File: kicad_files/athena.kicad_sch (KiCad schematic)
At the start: 619 parts, among them J1 TYPE-C-31-M-12, J2 A1001WR-S-04P, Q1 2N7002, Q2 2N7002, Q3 AO3401A, Q4 2N7002, Q5 2N7002, Q6 2N7002, Q7 2N7002, Q8 2N7002, SW1 K2-1187SQ-A4SW-06, SW10 MX Switch, SW100 MX Switch, SW101 MX Switch, SW102 MX Switch, SW103 MX Switch, SW104 MX Switch, SW105 MX Switch, SW106 MX Switch, SW107 MX Switch, SW108 MX Switch, SW109 MX Switch, SW11 MX Switch, SW110 MX Switch, SW111 MX Switch, SW112 MX Switch, SW113 MX Switch, SW114 MX Switch, SW115 MX Switch, SW116 MX Switch, SW117 MX Switch, SW118 MX Switch, SW119 MX Switch, SW12 MX Switch, SW120 MX Switch, SW13 MX Switch, SW14 MX Switch, SW15 MX Switch, SW16 MX Switch, SW17 MX Switch, SW18 MX Switch, SW19 MX Switch, SW2 MX Switch, SW20 MX Switch, SW21 MX Switch, SW22 MX Switch, SW23 MX Switch, SW24 MX Switch, SW25 MX Switch, SW26 MX Switch, SW27 MX Switch, SW28 MX Switch, SW29 MX Switch, SW3 MX Switch, SW30 MX Switch, SW31 MX Switch, SW32 MX Switch, SW33 MX Switch, SW34 MX Switch, SW35 MX Switch, SW36 MX Switch, SW37 MX Switch, SW38 MX Switch, SW39 MX Switch, SW4 MX Switch, SW40 MX Switch, SW41 MX Switch, SW42 MX Switch, SW43 MX Switch, SW44 MX Switch, SW45 MX Switch, SW46 MX Switch, SW47 MX Switch, SW48 MX Switch, SW49 MX Switch, SW5 MX Switch, SW50 MX Switch, SW51 MX Switch, SW52 MX Switch, SW53 MX Switch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

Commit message: DRC ran, no issues found,, schematic cleaned up
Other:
- note removed: "RGB STRIP"
- moved on the sheet: C18, C19, C20, C21, C22, C23, C24, C25, C26, C27, C28, C29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

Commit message: Adjustments for LDO and RGB level translator due to no stock
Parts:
- removed C12: 10n, Capacitor_SMD:C_0402_1005Metric, symbol Device:C_Small
- removed U4: SGM2007-3.3XN5/TR, acheron_Components:SOT-23-5, symbol acheron_Symbols:SGM2036
- added U4: AP7333, Package_TO_SOT_SMD:SOT-23, symbol acheron_Symbols:UR133AG-33_SOT-89-3
- U5: value TXS0101DRLR -> TXS0101DCKR; footprint acheron_Components:SOT-563 -> acheron_Components:SOT-363_SC-70-6; Manufacturer Part Number TXS0101DRLR -> TXS0101DCKR; Package SOT-563 -> SC-70-6; Vendor Part Number LCSC C131928 -> LCSC C132031
- X1: renamed from X4; now left out of the parts list
- X4: renamed from X3; now left out of the parts list
- renumbered C11 to C10, C13 to C11, C14 to C12, C15 to C13, C16 to C14, C17 to C15, C21 to C16, C22 to C17, C23 to C18, C24 to C19, C25 to C20, C26 to C21, C27 to C22, C28 to C23, C29 to C24, C30 to C25, C31 to C26, C32 to C27, C33 to C28, C34 to C29, C35 to C30, C36 to C31, C37 to C32, C18 to C33, C19 to C34, C20 to C35, C9 to C36, C38 to C37, C39 to C38, C40 to C39, C41 to C40, C42 to C41, C43 to C42, C44 to C43, C45 to C44, C46 to C45, C47 to C46, C48 to C47, C49 to C48, C50 to C49, C51 to C50, C10 to C9, D11 to D10, D113 to D100, D114 to D101, D115 to D102, D116 to D103, D118 to D105, D120 to D106, D121 to D107, D122 to D108, D123 to D109, D12 to D11, D124 to D110, D68 to D111, D125 to D112, D119 to D113, D132 to D114, D117 to D115, D133 to D116, D128 to D117, D127 to D118, D126 to D119, D13 to D12, D53 to D120, D52 to D121, D51 to D122, D70 to D123, D69 to D124, D85 to D125, D87 to D126, D86 to D127, D102 to D128, D131 to D129, D14 to D13, D129 to D131, D71 to D132, D15 to D14, D16 to D15, D17 to D16, D18 to D17, D19 to D18, D20 to D19, D21 to D20, D22 to D21, D23 to D22, D24 to D23, D25 to D24, D26 to D25, D27 to D26, D28 to D27, D29 to D28, D30 to D29, D4 to D3, D31 to D30, D32 to D31, D33 to D32, D34 to D33, D35 to D34, D36 to D35, D37 to D36, D38 to D37, D39 to D38, D40 to D39, D5 to D4, D41 to D40, D42 to D41, D43 to D42, D44 to D43, D45 to D44, D46 to D45, D47 to D46, D48 to D47, D49 to D48, D50 to D49, D6 to D5, D54 to D50, D55 to D51, D56 to D52, D57 to D53, D58 to D54, D59 to D55, D60 to D56, D61 to D57, D62 to D58, D63 to D59, D7 to D6, D64 to D60, D65 to D61, D66 to D62, D67 to D63, D72 to D64, D73 to D65, D74 to D66, D75 to D67, D76 to D68, D77 to D69, D8 to D7, D78 to D70, D79 to D71, D80 to D72, D81 to D73, D82 to D74, D83 to D75, D84 to D76, D88 to D77, D89 to D78, D90 to D79, D9 to D8, D91 to D80, D92 to D81, D93 to D82, D94 to D83, D95 to D84, D96 to D85, D97 to D86, D98 to D87, D99 to D88, D100 to D89, D10 to D9, D101 to D90, D103 to D91, D105 to D92, D106 to D93, D107 to D94, D108 to D95, D109 to D96, D110 to D97, D111 to D98, D112 to D99, FB3 to FB1, FB1 to FB2, GR11 to GR10, GR9 to GR11, GR10 to GR8, GR8 to GR9, LED28 to LED1, LED5 to LED10, LED95 to LED100, LED96 to LED101, LED97 to LED102, LED98 to LED103, LED99 to LED104, LED100 to LED105, LED101 to LED106, LED102 to LED107, LED103 to LED108, LED104 to LED109, LED6 to LED11, LED105 to LED110, LED106 to LED111, LED107 to LED112, LED108 to LED113, LED109 to LED114, LED110 to LED115, LED111 to LED116, LED114 to LED117, LED112 to LED118, LED113 to LED119, LED7 to LED12, LED8 to LED13, LED9 to LED14, LED10 to LED15, LED11 to LED16, LED12 to LED17, LED13 to LED18, LED14 to LED19, LED68 to LED2, LED16 to LED20, LED17 to LED21, LED18 to LED22, LED19 to LED23, LED20 to LED24, LED21 to LED25, LED22 to LED26, LED23 to LED27, LED24 to LED28, LED25 to LED29, LED69 to LED3, LED36 to LED30, LED27 to LED31, LED29 to LED32, LED30 to LED33, LED31 to LED34, LED32 to LED35, LED33 to LED36, LED34 to LED37, LED35 to LED38, LED37 to LED39, LED26 to LED4, LED38 to LED40, LED39 to LED41, LED40 to LED42, LED41 to LED43, LED42 to LED44, LED43 to LED45, LED44 to LED46, LED56 to LED47, LED45 to LED48, LED46 to LED49, LED3 to LED5, LED47 to LED50, LED48 to LED51, LED49 to LED52, LED50 to LED53, LED51 to LED54, LED52 to LED55, LED53 to LED56, LED54 to LED57, LED55 to LED58, LED57 to LED59, LED15 to LED6, LED58 to LED60, LED59 to LED61, LED60 to LED62, LED61 to LED63, LED62 to LED64, LED74 to LED65, LED67 to LED66, LED117 to LED67, LED63 to LED68, LED64 to LED69, LED1 to LED7, LED65 to LED70, LED66 to LED71, LED70 to LED72, LED71 to LED73, LED72 to LED74, LED73 to LED75, LED75 to LED76, LED76 to LED77, LED77 to LED78, LED118 to LED79, LED2 to LED8, LED119 to LED80, LED78 to LED81, LED79 to LED82, LED92 to LED83, LED93 to LED84, LED80 to LED85, LED81 to LED86, LED82 to LED87, LED83 to LED88, LED84 to LED89, LED4 to LED9, LED85 to LED90, LED86 to LED91, LED87 to LED92, LED88 to LED93, LED89 to LED94, LED90 to LED95, LED91 to LED96, LED115 to LED97, LED116 to LED98, LED94 to LED99, Q5 to Q3, Q6 to Q4, Q7 to Q5, Q8 to Q6, Q3 to Q7, Q4 to Q8, R11 to R10, R58 to R100, R59 to R101, R60 to R102, R61 to R103, R62 to R104, R64 to R105, R65 to R106, R66 to R107, R67 to R108, R68 to R109, R12 to R11, R69 to R110, R70 to R111, R71 to R112, R72 to R113, R63 to R114, R73 to R115, R75 to R116, R76 to R117, R77 to R118, R83 to R119, R10 to R12, R78 to R120, R80 to R121, R84 to R122, R85 to R123, R86 to R124, R81 to R125, R82 to R126, R145 to R127, R146 to R128, R87 to R129, R144 to R130, R79 to R131, R91 to R132, R93 to R133, R94 to R134, R89 to R135, R90 to R136, R95 to R137, R96 to R138, R97 to R139, R98 to R140, R99 to R141, R100 to R142, R101 to R143, R102 to R144, R103 to R145, R104 to R146, R105 to R147, R138 to R148, R141 to R149, R106 to R150, R107 to R151, R108 to R152, R109 to R153, R110 to R154, R111 to R155, R112 to R156, R113 to R157, R114 to R158, R115 to R159, R134 to R16, R116 to R160, R117 to R161, R135 to R17, R147 to R18, R148 to R19, R149 to R20, R150 to R21, R151 to R22, R152 to R23, R153 to R24, R154 to R25, R155 to R26, R156 to R27, R157 to R28, R158 to R29, R159 to R30, R160 to R31, R161 to R32, R16 to R33, R118 to R34, R119 to R35, R120 to R36, R121 to R37, R122 to R38, R123 to R39, R124 to R40, R125 to R41, R126 to R42, R127 to R43, R128 to R44, R129 to R45, R130 to R46, R131 to R47, R132 to R48, R133 to R49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
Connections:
- net 3V3: now also R11.2, U4.2 (VO); no longer R11.1
- net 5V: now also U4.1 (VI)
- net GND: now also R11.1, U4.3 (GND); no longer R11.2
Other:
- moved on the sheet: D100, D101, D102, D103, D104, D105, D106, D107, D108, D109, D110, D111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

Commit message: New DRC ran, no errors issued. Ready for release
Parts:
- R58, R59, R60, R61: Package R0402 -> R0805
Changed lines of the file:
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@@
     (title "Athena PCB schematic")
     (date "2023-04-26")
-    (rev "V3.0.2")
+    (rev "V3.0.3")
     (company "Acheron Project")
     (comment 1 "Designed by Gondolindrim")
@@
       (effects (font (size 1.27 1.27)) hide)
     )
-    (property "Package" "R0402" (at 279.4 412.75 0)
-      (effects (font (size 1.27 1.27)) hide)
-    )
     (property "Manufacturer" "Uniroyal" (at 279.4 412.75 0)
       (effects (font (size 1.27 1.27)) hide)
@@
       (effects (font (size 1.27 1.27)) hide)
     )
-    (property "Package" "R0402" (at 406.4 412.75 0)
-      (effects (font (size 1.27 1.27)) hide)
-    )
     (property "Manufacturer" "Uniroyal" (at 406.4 412.75 0)
       (effects (font (size 1.27 1.27)) hide)
@@
       (effects (font (size 1.27 1.27)) hide)
     )
-    (property "Package" "R0402" (at 342.9 412.75 0)
-      (effects (font (size 1.27 1.27)) hide)
-    )
     (property "Manufacturer" "Uniroyal" (at 342.9 412.75 0)
       (effects (font (size 1.27 1.27)) hide)
@@
       (effects (font (size 1.27 1.27)) hide)
     )
-    (property "Package" "R0402" (at 215.9 412.75 0)
-      (effects (font (size 1.27 1.27)) hide)
-    )

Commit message: Adjusted LDO footprint
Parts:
- removed U4: AP7333, Package_TO_SOT_SMD:SOT-23, symbol acheron_Symbols:UR133AG-33_SOT-89-3
- added U6: MCP1700T-3302E/TT, Package_TO_SOT_SMD:SOT-23, symbol Regulator_Linear:MCP1700-3302E_SOT23
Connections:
- net 3V3: now also U6.2 (VO)
- net 5V: now also U6.3 (VI)
- net GND: now also U6.1 (GND)
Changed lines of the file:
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@@
   (junction (at 424.815 565.15) (diameter 0) (color 0 0 0 0)
   )
-  (junction (at 908.05 406.4) (diameter 0) (color 0 0 0 0)
-  )
   (junction (at 793.75 419.1) (diameter 1.016) (color 0 0 0 0)
   )
@@
   (junction (at 1047.75 342.9) (diameter 1.016) (color 0 0 0 0)
   )
-  (junction (at 1035.05 434.34) (diameter 0) (color 0 0 0 0)
-  )
   (junction (at 1035.05 330.2) (diameter 0.9144) (color 0 0 0 0)
   )
@@
   (junction (at 189.865 447.04) (diameter 0.9144) (color 0 0 0 0)
   )
-  (junction (at 933.45 406.4) (diameter 0) (color 0 0 0 0)
-  )
   (junction (at 272.415 596.9) (diameter 0) (color 0 0 0 0)
   )
@@
     (stroke (width 0) (type default))
   )
-  (wire (pts (xy 908.05 406.4) (xy 911.86 406.4))
-    (stroke (width 0) (type solid))
-  )
   (wire (pts (xy 200.66 122.555) (xy 193.04 122.555))
     (stroke (width 0) (type solid))
@@
     (stroke (width 0) (type solid))
   )
-  (wire (pts (xy 908.05 406.4) (xy 908.05 408.94))
-    (stroke (width 0) (type solid))
-  )
   (wire (pts (xy 177.165 614.68) (xy 177.165 615.95))
     (stroke (width 0) (type solid))
@@
     (stroke (width 0) (type solid))
   )
-  (wire (pts (xy 1035.05 406.4) (xy 1035.05 434.34))
+  (wire (pts (xy 1035.05 406.4) (xy 1035.05 444.5))
     (stroke (width 0) (type default))
   )
@@
     (stroke (width 0) (type solid))
   )
-  (wire (pts (xy 1035.05 434.34) (xy 1035.05 444.5))
-    (stroke (width 0) (type default))
-  )
   (wire (pts (xy 1009.65 444.5) (xy 1009.65 482.6))
     (stroke (width 0) (type solid))
@@
     (stroke (width 0) (type solid))
   )
+  (wire (pts (xy 908.05 406.4) (xy 911.86 406.4))
+    (stroke (width 0) (type solid))
+  )
   (wire (pts (xy 139.065 438.15) (xy 139.065 440.69))
     (stroke (width 0) (type solid))
@@
     (stroke (width 0) (type solid))
   )
-  (wire (pts (xy 1034.415 434.34) (xy 1035.05 434.34))
-    (stroke (width 0) (type default))
-  )
   (wire (pts (xy 1060.45 635) (xy 1064.26 635))
     (stroke (width 0) (type solid))
@@
     (stroke (width 0) (type solid))
   )
-  (wire (pts (xy 520.7 114.3) (xy 520.7 115.57))
-    (stroke (width 0) (type solid))
-  )
   (wire (pts (xy 1014.73 255.27) (xy 1013.46 255.27))
     (stroke (width 0) (type solid))
@@
     (stroke (width 0) (type solid))
   )
-  (wire (pts (xy 933.45 406.4) (xy 933.45 408.94))
-    (stroke (width 0) (type solid))
-  )
   (wire (pts (xy 418.465 607.06) (xy 418.465 606.425))
     (stroke (width 0) (type default))
@@
     )
   )
+  (symbol (lib_id "Regulator_Linear:MCP1700-3302E_SOT23") (at 520.7 107.95 0) (unit 1)
+    (in_bom yes) (on_board yes) (dnp no)
+    (property "Reference" "U6" (at 520.7 101.6 0)
+      (effects (font (size 1.27 1.27)))
+    )
+    (property "Value" "MCP1700T-3302E/TT" (at 520.7 103.505 0)
+      (effects (font (size 0.762 0.762)))
+    )
+    (property "Footprint" "Package_TO_SOT_SMD:SOT-23" (at 520.7 102.235 0)
+      (effects (font (size 1.27 1.27)) hide)
+    )
+    (property "Datasheet" "http://ww1.microchip.com/downloads/en/DeviceDoc/20001826D.pdf" (at 520.7 107.95 0)
+      (effects (font (size 1.27 1.27)) hide)
+    )
+    (property "Manufacturer Part Number" "MCP1700T-3302E/TT" (at 520.7 107.95 0)
+      (effects (font (size 1.27 1.27)) hide)
+    )
+    (property "Manufacturer" "Microchip" (at 520.7 107.95 0)
+      (effects (font (size 1.27 1.27)) hide)
+    )
+    (property "Package" "SOT-23" (at 520.7 107.95 0)
+      (effects (font (size 1.27 1.27)) hide)
+    )
+    (property "LCSC Part Number" "" (at 520.7 107.95 0)
+      (effects (font (size 1.27 1.27)) hide)
+    )
+    (property "Specification" "3.3V fixed linear dropout regulator" (at 520.7 107.95 0)
+      (effects (font (size 1.27 1.27)) hide)
+    )
+    (property "Vendor Part Number" "LCSC C39051" (at 520.7 107.95 0)
+      (effects (font (size 1.27 1.27)) hide)
+    )
+    (pin "1")
+    (pin "2")
+    (pin "3")
+    (instances
+      (project "athena"
+        (path "/9ce6b20d-0a6c-402a-b232-5eafd6242eb3"
+          (reference "U6") (unit 1)
+        )
+      )
+      (project "themis87h"
+        (path "/cac53280-0cb3-46d1-85a6-feb33ccfa3b3"
+          (reference "U3") (unit 1)
+        )
+      )
+      (project "evolv"
+        (path "/e63e39d7-6ac0-4ffd-8aa3-1841a4541b55"
+          (reference "U1") (unit 1)
+        )
+      )
+    )
+  )
   (symbol (lib_id "Device:C_Small") (at 193.04 125.73 0) (unit 1)
     (in_bom yes) (on_board yes) (dnp no)
@@
         )
       )
-    )
-  )
-  (symbol (lib_id "acheron_Symbols:UR133AG-33_SOT-89-3") (at 520.7 107.95 0) (unit 1)
-    (in_bom yes) (on_board yes) (dnp no) (fields_autoplaced)
-    (property "Reference" "U4" (at 520.7 100.33 0)
-      (effects (font (size 1.27 1.27)))
-    )
-    (property "Value" "AP7333" (at 520.7 102.87 0)
-      (effects (font (size 1.27 1.27)))
-    )
-    (property "Footprint" "Package_TO_SOT_SMD:SOT-23" (at 520.7 97.79 0)
-      (effects (font (size 1.27 1.27)) hide)
-    )
-    (property "Datasheet" "" (at 520.7 107.95 0)
-      (effects (font (size 1.27 1.27)) hide)
-    )
-    (property "Package" "SOT-23" (at 520.7 107.95 0)
-      (effects (font (size 1.27 1.27)) hide)
-    )
-    (property "Manufacturer" "Diodes Incorporated" (at 520.7 107.95 0)
-      (effects (font (size 1.27 1.27)) hide)
-    )
-    (property "Manufacturer Part Number" "AP7333-33SRG-7" (at 520.7 107.95 0)
-      (effects (font (size 1.27 1.27)) hide)
-    )
-    (property "Vendor Part Number" "LCSC C150745" (at 520.7 107.95 0)
-      (effects (font (size 1.27 1.27)) hide)
-    )
-    (property "Specification" "300mA 65dB@(100Hz) Fixed 3.3V SOT-23 LDO" (at 520.7 107.95 0)
-      (effects (font (size 1.27 1.27)) hide)
-    )
-    (pin "1")
-    (pin "2")
-    (pin "3")
-    (instances
-      (project "athena"
-        (path "/9ce6b20d-0a6c-402a-b232-5eafd6242eb3"
-          (reference "U4") (unit 1)
-        )
-      )

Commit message: New grounding scheme on USB connector
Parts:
- removed FB2: GZ2012D601TF, Inductor_SMD:L_0805_2012Metric, symbol Device:Ferrite_Bead_Small
- added R16: 0R, Resistor_SMD:R_0805_2012Metric, symbol Device:R_Small
- renumbered D43 to D10, D44 to D11, D45 to D12, D46 to D13, D47 to D14, D48 to D15, D49 to D16, D3 to D17, D4 to D18, D5 to D19, D6 to D20, D7 to D21, D8 to D22, D9 to D23, D10 to D24, D11 to D25, D12 to D26, D13 to D27, D14 to D28, D15 to D29, D36 to D3, D16 to D30, D17 to D31, D18 to D32, D19 to D33, D50 to D34, D51 to D35, D52 to D36, D53 to D37, D54 to D38, D55 to D39, D37 to D4, D56 to D40, D57 to D41, D58 to D42, D59 to D43, D60 to D44, D61 to D45, D62 to D46, D63 to D47, D20 to D48, D21 to D49, D38 to D5, D22 to D50, D23 to D51, D24 to D52, D25 to D53, D26 to D54, D27 to D55, D28 to D56, D29 to D57, D30 to D58, D31 to D59, D39 to D6, D32 to D60, D33 to D61, D34 to D62, D35 to D63, D40 to D7, D41 to D8, D42 to D9, R99 to R100, R100 to R101, R101 to R102, R102 to R103, R103 to R104, R104 to R105, R105 to R106, R106 to R107, R107 to R108, R108 to R109, R109 to R110, R110 to R111, R111 to R112, R112 to R113, R113 to R114, R114 to R115, R115 to R116, R116 to R117, R117 to R118, R118 to R119, R119 to R120, R120 to R121, R121 to R122, R122 to R123, R123 to R124, R124 to R125, R125 to R126, R126 to R127, R127 to R128, R128 to R129, R129 to R130, R130 to R131, R131 to R132, R132 to R133, R133 to R134, R134 to R135, R135 to R136, R136 to R137, R137 to R138, R138 to R139, R139 to R140, R140 to R141, R141 to R142, R142 to R143, R143 to R144, R144 to R145, R145 to R146, R146 to R147, R147 to R148, R148 to R149, R149 to R150, R150 to R151, R151 to R152, R152 to R153, R153 to R154, R154 to R155, R155 to R156, R156 to R157, R157 to R158, R158 to R159, R159 to R160, R160 to R161, R161 to R162, R16 to R17, R17 to R18, R18 to R19, R19 to R20, R20 to R21, R21 to R22, R22 to R23, R23 to R24, R24 to R25, R25 to R26, R26 to R27, R27 to R28, R28 to R29, R29 to R30, R30 to R31, R31 to R32, R32 to R33, R33 to R34, R34 to R35, R35 to R36, R36 to R37, R37 to R38, R38 to R39, R39 to R40, R40 to R41, R41 to R42, R42 to R43, R43 to R44, R44 to R45, R45 to R46, R46 to R47, R47 to R48, R48 to R49, R49 to R50, R50 to R51, R51 to R52, R52 to R53, R53 to R54, R54 to R55, R55 to R56, R56 to R57, R57 to R58, R58 to R59, R59 to R60, R60 to R61, R61 to R62, R62 to R63, R63 to R64, R64 to R65, R65 to R66, R66 to R67, R67 to R68, R68 to R69, R69 to R70, R70 to R71, R71 to R72, R72 to R73, R73 to R74, R74 to R75, R75 to R76, R76 to R77, R77 to R78, R78 to R79, R79 to R80, R80 to R81, R81 to R82, R82 to R83, R83 to R84, R84 to R85, R85 to R86, R86 to R87, R87 to R88, R88 to R89, R89 to R90, R90 to R91, R91 to R92, R92 to R93, R93 to R94, R94 to R95, R95 to R96, R96 to R97, R97 to R98, R98 to R99, U6 to U4
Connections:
- net GND: now also R16.2; no longer J1.A1 (GND), J1.B1 (GND), R12.1, R14.2
- net GNDPWR renamed GND1
- net GND1: now also J1.A1 (GND), J1.B1 (GND), R12.1, R14.2, R16.1

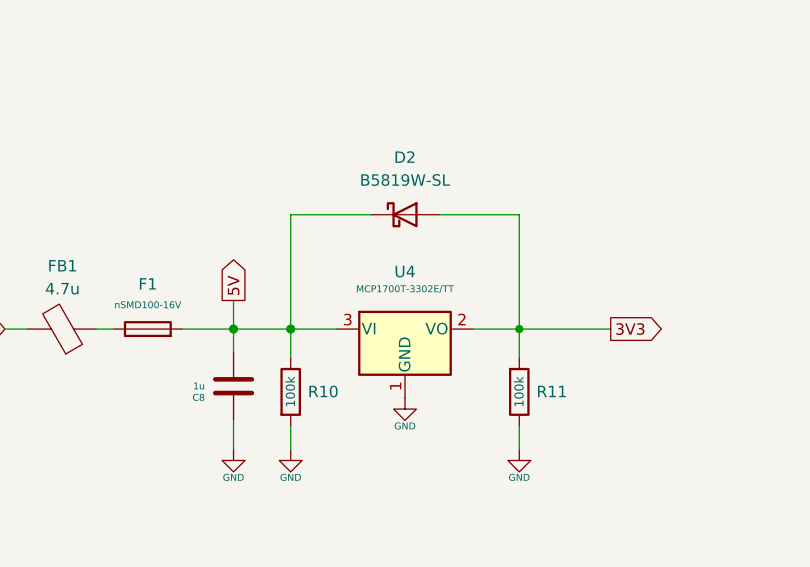
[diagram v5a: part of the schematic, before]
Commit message: New lighter SOT-23 footprint
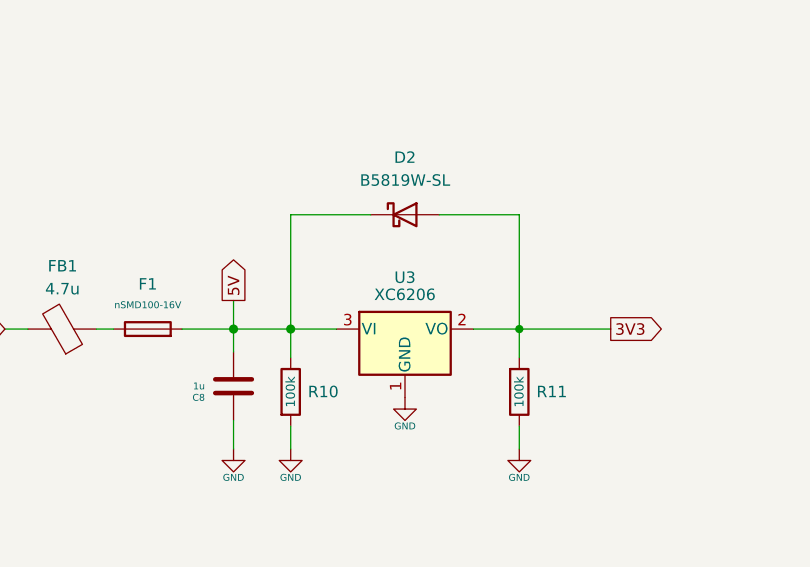
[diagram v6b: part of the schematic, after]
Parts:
- removed U4: MCP1700T-3302E/TT, Package_TO_SOT_SMD:SOT-23, symbol Regulator_Linear:MCP1700-3302E_SOT23
- added U3: XC6206, acheron_Components:SOT-23, symbol Regulator_Linear:MCP1700-3302E_SOT23
- Q1, Q2, Q3, Q4, Q5, Q6, Q7, Q8: footprint Package_TO_SOT_SMD:SOT-23 -> acheron_Components:SOT-23
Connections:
- net 3V3: now also U3.2 (VO)
- net 5V: now also U3.3 (VI)
- net GND: now also U3.1 (GND)
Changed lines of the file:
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@@
     )
   )
-  (symbol (lib_id "Regulator_Linear:MCP1700-3302E_SOT23") (at 520.7 107.95 0) (unit 1)
-    (in_bom yes) (on_board yes) (dnp no)
-    (property "Reference" "U4" (at 520.7 101.6 0)
-      (effects (font (size 1.27 1.27)))
-    )
-    (property "Value" "MCP1700T-3302E/TT" (at 520.7 103.505 0)
-      (effects (font (size 0.762 0.762)))
-    )
-    (property "Footprint" "Package_TO_SOT_SMD:SOT-23" (at 520.7 102.235 0)
-      (effects (font (size 1.27 1.27)) hide)
-    )
-    (property "Datasheet" "http://ww1.microchip.com/downloads/en/DeviceDoc/20001826D.pdf" (at 520.7 107.95 0)
-      (effects (font (size 1.27 1.27)) hide)
-    )
-    (property "Manufacturer Part Number" "MCP1700T-3302E/TT" (at 520.7 107.95 0)
-      (effects (font (size 1.27 1.27)) hide)
-    )
-    (property "Manufacturer" "Microchip" (at 520.7 107.95 0)
-      (effects (font (size 1.27 1.27)) hide)
-    )
-    (property "Package" "SOT-23" (at 520.7 107.95 0)
-      (effects (font (size 1.27 1.27)) hide)
-    )
-    (property "LCSC Part Number" "" (at 520.7 107.95 0)
-      (effects (font (size 1.27 1.27)) hide)
-    )
-    (property "Specification" "3.3V fixed linear dropout regulator" (at 520.7 107.95 0)
-      (effects (font (size 1.27 1.27)) hide)
-    )
-    (property "Vendor Part Number" "LCSC C39051" (at 520.7 107.95 0)
-      (effects (font (size 1.27 1.27)) hide)
-    )
-    (pin "1")
-    (pin "2")
-    (pin "3")
-    (instances
-      (project "athena"
-        (path "/9ce6b20d-0a6c-402a-b232-5eafd6242eb3"
-          (reference "U4") (unit 1)
-        )
-      )
-      (project "themis87h"
-        (path "/cac53280-0cb3-46d1-85a6-feb33ccfa3b3"
-          (reference "U3") (unit 1)
-        )
-      )
-      (project "evolv"
-        (path "/e63e39d7-6ac0-4ffd-8aa3-1841a4541b55"
-          (reference "U1") (unit 1)
-        )
-      )
-    )
-  )
   (symbol (lib_id "Device:C_Small") (at 193.04 125.73 0) (unit 1)
     (in_bom yes) (on_board yes) (dnp no)
@@
       (effects (font (size 1.27 1.27)) (justify left))
     )
-    (property "Footprint" "Package_TO_SOT_SMD:SOT-23" (at 358.14 408.305 0)
+    (property "Footprint" "acheron_Components:SOT-23" (at 358.14 408.305 0)
       (effects (font (size 1.27 1.27) italic) (justify left) hide)
     )
@@
       (effects (font (size 1.27 1.27)) (justify left))
     )
-    (property "Footprint" "Package_TO_SOT_SMD:SOT-23" (at 72.39 440.055 0)
+    (property "Footprint" "acheron_Components:SOT-23" (at 72.39 440.055 0)
       (effects (font (size 1.27 1.27) italic) (justify left) hide)
     )
@@
       (effects (font (size 1.27 1.27)) (justify left))
     )
-    (property "Footprint" "Package_TO_SOT_SMD:SOT-23" (at 103.505 423.545 0)
+    (property "Footprint" "acheron_Components:SOT-23" (at 103.505 423.545 0)
       (effects (font (size 1.27 1.27) italic) (justify left) hide)
     )
@@
       (effects (font (size 1.27 1.27)) (justify left))
     )
-    (property "Footprint" "Package_TO_SOT_SMD:SOT-23" (at 294.64 408.305 0)
+    (property "Footprint" "acheron_Components:SOT-23" (at 294.64 408.305 0)
       (effects (font (size 1.27 1.27) italic) (justify left) hide)
     )
@@
     )
   )
+  (symbol (lib_id "Regulator_Linear:MCP1700-3302E_SOT23") (at 520.7 107.95 0) (unit 1)
+    (in_bom yes) (on_board yes) (dnp no)
+    (property "Reference" "U3" (at 520.7 102.235 0)
+      (effects (font (size 1.27 1.27)))
+    )
+    (property "Value" "XC6206" (at 520.7 104.14 0)
+      (effects (font (size 1.27 1.27)))
+    )
+    (property "Footprint" "acheron_Components:SOT-23" (at 520.7 102.235 0)
+      (effects (font (size 1.27 1.27)) hide)
+    )
+    (property "Datasheet" "" (at 520.7 107.95 0)
+      (effects (font (size 1.27 1.27)) hide)
+    )
+    (property "Manufacturer Part Number" "XC6206P332MR" (at 520.7 107.95 0)
+      (effects (font (size 1.27 1.27)) hide)
+    )
+    (property "Manufacturer" "TOREX" (at 520.7 107.95 0)
+      (effects (font (size 1.27 1.27)) hide)
+    )
+    (property "Package" "SOT-23" (at 520.7 107.95 0)
+      (effects (font (size 1.27 1.27)) hide)
+    )
+    (property "LCSC Part Number" "" (at 520.7 107.95 0)
+      (effects (font (size 1.27 1.27)) hide)
+    )
+    (property "Specification" "3.3V fixed linear dropout regulator" (at 520.7 107.95 0)
+      (effects (font (size 1.27 1.27)) hide)
+    )
+    (property "Vendor Part Number" "LCSC C5446" (at 520.7 107.95 0)
+      (effects (font (size 1.27 1.27)) hide)
+    )
+    (pin "1")
+    (pin "2")
+    (pin "3")
+    (instances
+      (project "iron-ergo"
+        (path "/331f4312-89d6-48bf-abcc-ca6223e1392c"
+          (reference "U3") (unit 1)
+        )
+      )
+      (project "athena"
+        (path "/9ce6b20d-0a6c-402a-b232-5eafd6242eb3"
+          (reference "U4") (unit 1)
+        )
+      )
+      (project "themis87h"
+        (path "/cac53280-0cb3-46d1-85a6-feb33ccfa3b3"
+          (reference "U3") (unit 1)
+        )
+      )
+      (project "evolv"
+        (path "/e63e39d7-6ac0-4ffd-8aa3-1841a4541b55"
+          (reference "U1") (unit 1)
+        )
+      )
+    )
+  )
   (symbol (lib_id "Device:D") (at 895.35 351.79 270) (unit 1)
     (in_bom yes) (on_board yes) (dnp no)
@@
       (effects (font (size 1.27 1.27)) (justify left))
     )
-    (property "Footprint" "Package_TO_SOT_SMD:SOT-23" (at 653.415 93.98 0)
+    (property "Footprint" "acheron_Components:SOT-23" (at 653.415 93.98 0)
       (effects (font (size 1.27 1.27) italic) (justify left) hide)
     )
@@
       (effects (font (size 1.27 1.27)) (justify left))
     )
-    (property "Footprint" "Package_TO_SOT_SMD:SOT-23" (at 231.14 408.305 0)
+    (property "Footprint" "acheron_Components:SOT-23" (at 231.14 408.305 0)
       (effects (font (size 1.27 1.27) italic) (justify left) hide)
     )
@@
       (effects (font (size 1.27 1.27)) (justify left))
     )
-    (property "Footprint" "Package_TO_SOT_SMD:SOT-23" (at 421.64 408.305 0)
+    (property "Footprint" "acheron_Components:SOT-23" (at 421.64 408.305 0)
       (effects (font (size 1.27 1.27) italic) (justify left) hide)
     )
@@
       (effects (font (size 1.27 1.27)) (justify left))
     )
-    (property "Footprint" "Package_TO_SOT_SMD:SOT-23" (at 635 116.205 0)
+    (property "Footprint" "acheron_Components:SOT-23" (at 635 116.205 0)
       (effects (font (size 1.27 1.27) italic) (justify left) hide)
     )
